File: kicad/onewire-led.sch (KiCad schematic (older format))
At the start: 11 parts, among them IC1 ATTINY13A-P, P1 CONN_2

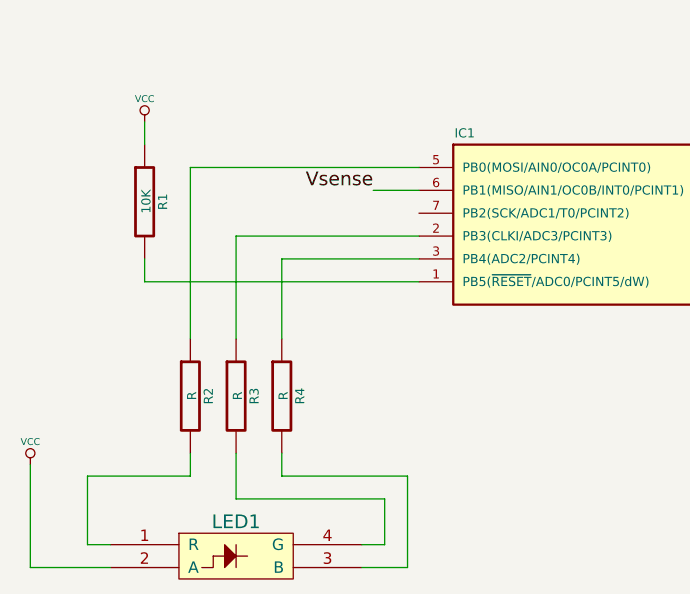
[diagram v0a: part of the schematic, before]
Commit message: Fixed layout for package sizes and incorrect PLCC layout
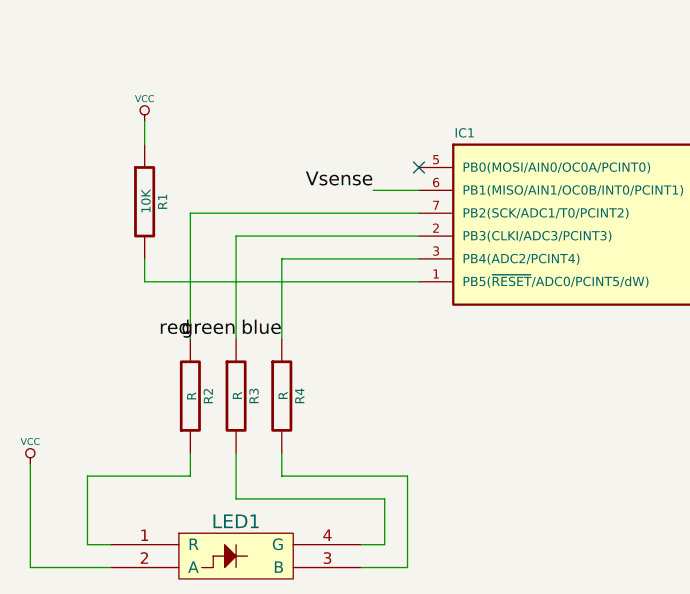
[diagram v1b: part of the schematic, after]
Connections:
- net green: now reaches IC1.2 (PB3(CLKI/ADC3/PCINT3)), R3.1
- net blue: now reaches IC1.3 (PB4(ADC2/PCINT4)), R4.1
- net at IC1.5 (PB0(MOSI/AIN0/OC0A/PCINT0)): no longer R2.1
- net red: now reaches IC1.7 (PB2(SCK/ADC1/T0/PCINT2))
- net red: now also R2.2
- net at LED1.1 (R): now also R2.1; no longer R2.2
- no-connect marks 0 -> 1
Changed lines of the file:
@@
 F 3 "~" H 3300 3900 30  0000 C CNN
 	1    3300 3900
-	1    0    0    -1
+	1    0    0    1
 $EndComp
 $Comp
@@
 	1    0    0    -1
 $EndComp
+Text Label 3300 3650 2    60   ~ 0
+red
+Text Label 3500 3650 2    60   ~ 0
+green
+Text Label 3700 3650 2    60   ~ 0
+blue
+Wire Wire Line
+	3300 3100 4300 3100
+Wire Wire Line
+	3300 3650 3300 3100
+Connection ~ 8700 2900
+Wire Wire Line
+	8550 2800 8550 2900
+Wire Wire Line
+	3100 2700 3100 2800
+Wire Wire Line
+	4250 4650 4050 4650
+Wire Wire Line
+	4250 4250 4250 4650
+Wire Wire Line
+	3700 4250 4250 4250
+Wire Wire Line
+	3700 4150 3700 4250
+Wire Wire Line
+	3500 4350 3500 4150
+Wire Wire Line
+	4150 4350 3500 4350
+Wire Wire Line
+	4150 4550 4150 4350
+Wire Wire Line
+	4050 4550 4150 4550
+Wire Wire Line
+	3300 4250 3300 4150
+Wire Wire Line
+	2850 4250 3300 4250
+Wire Wire Line
+	2850 4550 2850 4250
+Wire Wire Line
+	2950 4550 2850 4550
+Wire Wire Line
+	2600 4650 2950 4650
+Wire Wire Line
+	2600 4200 2600 4650
+Wire Wire Line
+	3100 3400 3100 3300
+Wire Wire Line
+	3500 3200 3500 3650
+Wire Wire Line
+	4300 3200 3500 3200
+Wire Wire Line
+	4100 3000 4300 3000
+Wire Wire Line
+	6400 2900 6300 2900
+Wire Wire Line
+	6400 2800 6400 2900
+Connection ~ 8200 2400
+Wire Wire Line
+	8300 2400 8200 2400
+Connection ~ 8200 3100
+Wire Wire Line
+	8200 2300 8200 2500
+Wire Wire Line
+	8200 1700 8200 1800
+Wire Wire Line
+	8200 3100 8800 3100
+Wire Wire Line
+	8200 3000 8200 3400
+Wire Wire Line
+	8200 3400 7900 3400
+Wire Wire Line
+	7400 2900 7400 2800
+Wire Wire Line
+	8700 2900 8700 2800
+Wire Wire Line
+	8550 2900 8800 2900
+Connection ~ 7400 3400
+Wire Wire Line
+	7200 3400 7500 3400
+Wire Wire Line
+	7400 3300 7400 3500
+Wire Wire Line
+	6400 3400 6300 3400
 Wire Wire Line
 	6400 3500 6400 3400
 Wire Wire Line
-	6400 3400 6300 3400
-Wire Wire Line
-	7400 3300 7400 3500
-Wire Wire Line
-	7200 3400 7500 3400
-Connection ~ 7400 3400
-Wire Wire Line
-	8550 2900 8800 2900
-Wire Wire Line
-	8700 2900 8700 2800
-Wire Wire Line
-	7400 2900 7400 2800
-Wire Wire Line
-	8200 3400 7900 3400
-Wire Wire Line
-	8200 3000 8200 3400
-Wire Wire Line
-	8200 3100 8800 3100
-Wire Wire Line
-	8200 1700 8200 1800
-Wire Wire Line
-	8200 2300 8200 2500
-Connection ~ 8200 3100
-Wire Wire Line
-	8300 2400 8200 2400
-Connection ~ 8200 2400
-Wire Wire Line
-	6400 2800 6400 2900
-Wire Wire Line
-	6400 2900 6300 2900
-Wire Wire Line
-	4100 3000 4300 3000
-Wire Wire Line
-	3300 2900 3300 3650
-Wire Wire Line
-	4300 3200 3500 3200
-Wire Wire Line
-	3500 3200 3500 3650
+	4300 3400 3100 3400
 Wire Wire Line
 	4300 3300 3700 3300
 Wire Wire Line
 	3700 3300 3700 3650
-Wire Wire Line
-	4300 3400 3100 3400
-Wire Wire Line
-	3100 3400 3100 3300
-Wire Wire Line
-	2600 4200 2600 4650
-Wire Wire Line
-	2600 4650 2950 4650
-Wire Wire Line
-	2950 4550 2850 4550
-Wire Wire Line
-	2850 4550 2850 4250
-Wire Wire Line
-	2850 4250 3300 4250
-Wire Wire Line
-	3300 4250 3300 4150
-Wire Wire Line
-	4050 4550 4150 4550
-Wire Wire Line
-	4150 4550 4150 4350
-Wire Wire Line
-	4150 4350 3500 4350
-Wire Wire Line
-	3500 4350 3500 4150
-Wire Wire Line
-	3700 4150 3700 4250
-Wire Wire Line
-	3700 4250 4250 4250
-Wire Wire Line
-	4250 4250 4250 4650
-Wire Wire Line
-	4250 4650 4050 4650
-Wire Wire Line
-	3100 2700 3100 2800
-Wire Wire Line
-	8550 2800 8550 2900
-Connection ~ 8700 2900
-Wire Wire Line
-	4300 2900 3300 2900
+NoConn ~ 4300 2900
 $EndSCHEMATC
